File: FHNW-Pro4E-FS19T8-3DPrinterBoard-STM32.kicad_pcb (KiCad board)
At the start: 4 copper layers, 155 x 95 mm, 209 parts, among them J101 Screw_Terminal_01x02, J201 Micro_SD_Card_Det, J202 Conn_02x05_Odd_Even, J204 Conn_ARM_JTAG_SWD_10, J401 Conn_01x02, J402 Conn_01x02, J403 Screw_Terminal_01x02, J404 Conn_01x02, J405 Conn_01x02, J406 Screw_Terminal_01x02, J407 Conn_01x02, J408 Conn_01x02, J409 Conn_01x02, J410 Conn_01x02, J411 Conn_01x02, J504 USB_C_Receptacle, J601 B4B-XH-A, J602 B4B-XH-A, J603 B4B-XH-A, J604 B4B-XH-A, Q1 2N3904, Q2 2N3904, SW201 SW_Push, SW301 SW_Push, SW302 SW_Push, T401 BUK963R3-60E, T402 BUK963R3-60E, T403 BUK963R3-60E, T404 BUK963R3-60E, T405 BUK963R3-60E, U1 USBLC6-2SC6, U101 LM2675M-3.3, U102 LM2675M-5, U201 STM32F103ZETx, U202 NTS0104PW-Q100J, U203 NTS0104PW-Q100J, U301 ESP32-WROOM-32, U502 FT2232D, U601 TMC2660, U602 TMC2660, U603 TMC2660, U604 TMC2660, X201 SG-210STF, X501 SG5032CCN-6.000000M-HJGA3

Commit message: added cache.lib to git
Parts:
- added J203: Conn_02x20_Top_Bottom, Connector_PinHeader_2.54mm:PinHeader_2x20_P2.54mm_Vertical, F.Cu at (184.2, 113.0)
- added R217: 200R, Resistors_SMD:R_0603, F.Cu at (206.4, 26.0)
- J204: footprint Connectors_Multicomp:Multicomp_MC9A12-2034_2x10x2.54mm_Straight -> Connector_PinHeader_1.27mm:PinHeader_2x05_P1.27mm_Vertical
- U101: footprint Housings_SOIC:SOIC-8-1EP_3.9x4.9mm_Pitch1.27mm -> Package_SO:SOIC-8_3.9x4.9mm_P1.27mm
- moved J204 90.9 mm to (211.5, 22.2), turned to 270 degrees
- moved R204 34.8 mm to (207.6, 29.8), turned to 270 degrees
- moved R212 32.5 mm to (207.6, 26.0), turned to 270 degrees
- moved D103 31.8 mm to (146.1, 66.7)
- moved C109 31.7 mm to (149.2, 61.0)
- moved U102 31.7 mm to (145.4, 60.3)
- moved C107 31.7 mm to (137.8, 55.2)
- moved C108 31.7 mm to (137.8, 66.7)
- moved L102 31.7 mm to (155.6, 60.3)
- moved R101 28.6 mm to (108.0, 59.1)
- moved R210 28.6 mm to (211.5, 26.0), turned to 270 degrees
- moved D102 28.6 mm to (108.0, 62.9)
- moved R211 27.3 mm to (208.9, 26.0), turned to 270 degrees
- moved R201 22.6 mm to (206.4, 29.8), turned to 90 degrees
- moved R207 19.1 mm to (218.4, 97.8)
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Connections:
- J204 pad 10: JTAG_RESET -> Net-(J204-Pad10)
- R203 pad 1: Net-(J204-Pad2) -> JTAG_TMS_SWDIO
- R204 pad 1: Net-(J204-Pad8) -> JTAG_TDI
- R205 pad 2: Net-(J204-Pad4) -> JTAG_TCK_SWCLK
- R206 pad 2: Net-(J204-Pad6) -> JTAG_TDO_SWO
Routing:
- net +3V3: track 77.4 -> 172.2 mm
- net /appendix_TMC2660_X/TMC_CS_X: track 5.21 -> 31.0 mm
- net /appendix_STM32F103/CS_Y: track 5.21 -> 31.0 mm
- net /appendix_STM32F103/CS_Z1: track 5.21 -> 31.0 mm
- net /appendix_STM32F103/EN_Y: track 3.58 -> 27.5 mm
- net /appendix_STM32F103/EN_Z1: track 3.58 -> 27.5 mm
- net /appendix_TMC2660_X/TMC_EN_X: track 3.58 -> 27.5 mm
- net Net-(D102-Pad2): track 3.73 -> 0.00 mm
- net GND: track 182.8 -> 186.5 mm, vias 80 -> 76
- net JTAG_TMS_SWDIO: track 0.00 -> 2.31 mm, vias 0 -> 1
- net JTAG_TDO_SWO: track 0.00 -> 2.31 mm, vias 0 -> 1
- net JTAG_TDI: track 0.00 -> 2.31 mm, vias 0 -> 1
- net JTAG_TCK_SWCLK: track 0.00 -> 2.31 mm, vias 0 -> 1
- net JTAG_RESET: track 0.00 -> 2.31 mm, vias 0 -> 1
- net Net-(J204-Pad8): track 0.00 -> 1.79 mm
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
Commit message: cleaned up Layout
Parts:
- removed R202: 100k, Resistors_SMD:R_0603
- T401, T404, T405: value BUK963R3-60E -> PMV40UN2; footprint Package_TO_SOT_SMD:TO-263-2 -> Package_TO_SOT_SMD:SOT-23
- moved R102 194.6 mm to (108.0, 57.1), turned to 270 degrees
- moved D104 192.1 mm to (108.0, 61.0), turned to 90 degrees
- moved R422 177.1 mm to (50.8, 58.4)
- moved D405 140.0 mm to (147.3, 30.5)
- moved R423 138.9 mm to (78.1, 55.9)
- moved J409 108.7 mm to (154.3, 25.4)
- moved T404 107.7 mm to (157.5, 34.9)
- moved J401 105.5 mm to (162.6, 25.4)
- moved R506 105.1 mm to (222.2, 79.4), turned to 180 degrees
- moved T401 104.2 mm to (165.7, 34.9)
- moved R413 103.7 mm to (154.3, 38.1), turned to 0 degrees
- moved R404 100.3 mm to (162.6, 38.1), turned to 0 degrees
- moved T405 89.7 mm to (149.2, 34.9), turned to 90 degrees
- moved R420 84.4 mm to (146.1, 38.1)
- moved X201 78.0 mm to (172.1, 51.4), turned to 270 degrees
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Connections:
- C613 pad 1: +3V3 -> +3.3VP
- C615 pad 1: +3V3 -> +3.3VP
- C629 pad 1: +3V3 -> +3.3VP
- C631 pad 1: +3V3 -> +3.3VP
- T401 pad 2: /appendix_SENSORS_POWER/Fan1_pwr -> GND
- T401 pad 3: GND -> /appendix_SENSORS_POWER/Fan1_pwr
- T404 pad 2: /appendix_SENSORS_POWER/Fan2_pwr -> GND
- T404 pad 3: GND -> /appendix_SENSORS_POWER/Fan2_pwr
- T405 pad 2: /appendix_SENSORS_POWER/Fan3_pwr -> GND
- T405 pad 3: GND -> /appendix_SENSORS_POWER/Fan3_pwr
- U601 pad 40: +3V3 -> +3.3VP
- U602 pad 40: +3V3 -> +3.3VP
- U603 pad 40: +3V3 -> +3.3VP
- U604 pad 40: +3V3 -> +3.3VP
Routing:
- net +3.3VP: track 0.00 -> 121.1 mm, vias 0 -> 5
- net GND: track 186.5 -> 270.9 mm
- net +3V3: track 172.2 -> 90.6 mm, vias 4 -> 0
- net +24V: track 35.0 -> 20.4 mm
- net Net-(C302-Pad1): track 0.00 -> 12.4 mm
- net /appendix_ESP32/ESP32_RESET: track 25.1 -> 36.8 mm
- net /SW_Min_Z: track 0.00 -> 7.25 mm
- net /SW_End_Filament1: track 0.00 -> 7.25 mm
- net /SW_Min_X: track 0.00 -> 7.14 mm
- net /ADC_TEMP_E1: track 0.00 -> 7.14 mm
- net /SW_Min_Y: track 0.00 -> 7.14 mm
- net /ADC_TEMP_BED: track 0.00 -> 7.14 mm
- net +5V: track 46.2 -> 52.8 mm
- net JTAG_RESET: track 2.31 -> 6.41 mm
- net Net-(R503-Pad1): track 4.18 -> 8.21 mm
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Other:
- board size 155 x 95 mm -> 152 x 95 mm
- board text added: "Fan 3"
- board text added: "OPTIONS"
- board text added: "RESET"
- board text added: "Temp Bed"
- board text added: "Temp Ext"
- board text removed: "3D Printer"
- board text removed: "ADC Bed"
- board text removed: "ADC E1"

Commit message: Layout update
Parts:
- added D201: LED, LED_SMD:LED_0805_2012Metric, F.Cu at (156.7, 42.2)
- added H101: MountingHole, Mounting_Holes:MountingHole_3.2mm_M3_Pad, F.Cu at (86.0, 24.0)
- added H102: MountingHole, Mounting_Holes:MountingHole_3.2mm_M3_Pad, F.Cu at (86.0, 111.0)
- added H103: MountingHole, Mounting_Holes:MountingHole_3.2mm_M3_Pad, F.Cu at (236.0, 24.0)
- added H104: MountingHole, Mounting_Holes:MountingHole_3.2mm_M3_Pad, F.Cu at (236.0, 111.0)
- added R202: 330R, Resistors_SMD:R_0603, F.Cu at (160.7, 41.9)
- J203: value Conn_02x20_Top_Bottom -> Conn_02x20_Odd_Even
- moved R411 90.8 mm to (139.7, 47.0), turned to 0 degrees
- moved T403 79.6 mm to (129.1, 44.5), turned to 180 degrees
- moved R415 73.8 mm to (144.8, 44.5), turned to 180 degrees
- moved C407 70.5 mm to (141.6, 43.2), turned to 90 degrees
- moved TH401 68.3 mm to (139.1, 43.2), turned to 270 degrees
- moved R422 67.5 mm to (114.3, 35.6), turned to 180 degrees
- moved R416 56.5 mm to (114.3, 37.5), turned to 0 degrees
- moved D401 54.0 mm to (109.9, 37.5), turned to 0 degrees
- moved J406 50.8 mm to (104.8, 26.7)
- moved R417 37.8 mm to (95.9, 37.5), turned to 0 degrees
- moved D402 37.6 mm to (92.7, 37.5), turned to 0 degrees
- moved T402 36.9 mm to (111.1, 44.5), turned to 0 degrees
- moved F401 29.3 mm to (87.6, 48.3), turned to 0 degrees
- moved D403 29.3 mm to (134.6, 28.6)
- moved J401 29.3 mm to (133.4, 23.5)
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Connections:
- J203 pad 10: Net-(J203-Pad10) -> MISO
- J203 pad 11: Net-(J203-Pad11) -> SCK
- J203 pad 18: GND -> Net-(J203-Pad18)
- J203 pad 19: GND -> Net-(J203-Pad19)
- J203 pad 20: GND -> Net-(J203-Pad20)
- J203 pad 21: +24V -> Net-(J203-Pad21)
- J203 pad 22: +24V -> Net-(J203-Pad22)
- J203 pad 23: +5V -> Net-(J203-Pad23)
- J203 pad 24: +3V3 -> Net-(J203-Pad24)
- J203 pad 25: MISO -> Net-(J203-Pad25)
- J203 pad 3: +5V -> +24V
- J203 pad 35: Net-(J203-Pad35) -> GND
- J203 pad 36: Net-(J203-Pad36) -> GND
- J203 pad 37: Net-(J203-Pad37) -> GND
- J203 pad 4: +3V3 -> +24V
- J203 pad 5: MOSI -> +5V
- J203 pad 6: SCK -> +5V
- J203 pad 7: Net-(J203-Pad7) -> +3V3
- J203 pad 8: Net-(J203-Pad8) -> +3V3
- J203 pad 9: Net-(J203-Pad9) -> MOSI
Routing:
- net +24V: track 20.4 -> 208.5 mm
- net /POWER_BED: track 0.00 -> 90.4 mm
- net /appendix_TMC2660_X/TMC_STEP_X: track 3.92 -> 87.6 mm
- net /appendix_TMC2660_X/TMC_STALL_X: track 6.57 -> 87.8 mm
- net /appendix_TMC2660_X/TMC_DIR_X: track 5.91 -> 86.4 mm
- net /POWER_E1: track 0.00 -> 71.8 mm
- net /appendix_TMC2660_X/TMC_EN_X: track 27.5 -> 94.8 mm
- net JTAG_TMS_SWDIO: track 2.31 -> 68.8 mm, vias 1 -> 2
- net /appendix_TMC2660_X/TMC_CS_X: track 31.0 -> 97.0 mm
- net /appendix_STM32F103/STEP_Y: track 3.92 -> 64.5 mm
- net SD_DAT0: track 4.73 -> 64.7 mm, vias 1 -> 2
- net /appendix_STM32F103/STALL_Y: track 6.57 -> 64.8 mm
- net SD_DAT1: track 4.39 -> 62.4 mm, vias 1 -> 2
- net /appendix_STM32F103/DIR_Y: track 5.91 -> 63.3 mm
- net JTAG_TCK_SWCLK: track 2.31 -> 57.3 mm, vias 1 -> 2
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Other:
- board size 152 x 95 mm -> 158 x 95 mm
- net class Default: clearance 0.2 -> 0.1
- net class Power 24V added: clearance 0.2, trace_width 1.2, via_dia 1.4, via_drill 1
- net class thick removed
- rule trace_clearance: 0.2 -> 0.1
- board text added: "EXT"
- board text added: "RST"
- board text added: "SWD"
- board text removed: "E1"

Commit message: having issues with netclasses
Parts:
- added C110: TBD, Capacitors_SMD:C_0603, F.Cu at (109.9, 71.8)
- added C214: 100n, Capacitors_SMD:C_0603, F.Cu at (185.3, 42.0)
- added D105: D_Zener, Diodes_SMD:D_SMB, F.Cu at (109.9, 59.1)
- added R103: TBD, Resistors_SMD:R_0603, F.Cu at (106.0, 58.4)
- added T101: BUK963R3-60E, Package_TO_SOT_SMD:TO-263-2, F.Cu at (104.1, 66.0)
- moved C105 63.3 mm to (136.9, 1.27)
- moved C106 63.3 mm to (136.9, 2.54)
- moved FB102 63.3 mm to (134.3, 4.45)
- moved FB101 63.3 mm to (134.3, -0.64)
- moved D102 50.2 mm to (146.7, 51.1), turned to 180 degrees
- moved R101 45.8 mm to (142.9, 51.1), turned to 0 degrees
- moved F101 12.1 mm to (96.9, 57.1)
- moved C108 11.1 mm to (116.2, 66.7)
- moved C107 9.81 mm to (114.9, 55.2)
- moved R102 9.21 mm to (109.9, 53.7), turned to 180 degrees
- moved D104 8.67 mm to (106.0, 53.7), turned to 0 degrees
- moved D103 8.38 mm to (121.8, 66.7)
- moved L102 8.38 mm to (131.3, 60.3)
- moved C109 8.38 mm to (124.9, 61.0)
- moved U102 8.38 mm to (121.1, 60.3)
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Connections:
- net /ADC_TEMP_BED renamed /ADC_T_BED
- net /ADC_TEMP_E1 renamed /ADC_T_E1
- net /ADC_TEMP_PCB renamed /ADC_T_PCB
- net /POWER_BED renamed /BED_ON
- net /POWER_E1 renamed /E1_ON
- net Net-(J203-Pad12) renamed GPIO_EXT_0
- net Net-(J203-Pad13) renamed E3_CS
- net Net-(J203-Pad14) renamed E2_CS
- net Net-(J203-Pad15) renamed E3_STEP
- net Net-(J203-Pad16) renamed E2_STEP
- net Net-(J203-Pad17) renamed E3_DIR
- net Net-(J203-Pad18) renamed ES_DIR
- net Net-(J203-Pad19) renamed E3_EN
- net Net-(J203-Pad20) renamed E2_EN
- net Net-(J203-Pad21) renamed E3_STALL
- net Net-(J203-Pad22) renamed E2_STALL
- net Net-(J203-Pad23) renamed E3_END_FIL
- net Net-(J203-Pad24) renamed E2_END_FIL
- net Net-(J203-Pad25) renamed E3_ADC_TEMP
- net Net-(J203-Pad26) renamed E2_ADC_TEMP
- net Net-(J203-Pad27) renamed ADC_TEMP_EXT
- net Net-(J203-Pad28) renamed FAN_EXT
- net Net-(J203-Pad29) renamed GPIO_EXT_1
- net Net-(J203-Pad30) renamed E2_FAN1
- net Net-(J203-Pad31) renamed GPIO_EXT_2
- net Net-(J203-Pad32) renamed E2_FAN2
- net Net-(J203-Pad33) renamed GPIO_EXT_3
- net Net-(J203-Pad34) renamed E2_HOTEND
- net Net-(U201-Pad28) renamed /appendix_STM32F103/ADC_T_BED
- net Net-(U201-Pad29) renamed /appendix_STM32F103/ADC_T_E1
- net Net-(U201-Pad70) renamed /appendix_STM32F103/BED_ON
- F101 pad 2: Net-(F101-Pad2) -> Net-(C110-Pad1)
- J101 pad 1: Net-(F101-Pad2) -> Net-(J101-Pad1)
- J101 pad 2: GND -> Net-(C110-Pad1)
- J203 pad 5: +5V -> Net-(J203-Pad5)
- J203 pad 6: +5V -> Net-(J203-Pad6)
- R401 pad 1: +3V3 -> +3.3VA
- R405 pad 1: +3V3 -> +3.3VA
- R415 pad 1: +3V3 -> +3.3VA
- U201 pad 11: Net-(U201-Pad11) -> /appendix_STM32F103/CS_X
- U201 pad 12: Net-(U201-Pad12) -> /appendix_STM32F103/EN_X
- U201 pad 13: Net-(U201-Pad13) -> /appendix_STM32F103/STALL_X
- U201 pad 14: Net-(U201-Pad14) -> /appendix_STM32F103/DIR_X
- U201 pad 15: Net-(U201-Pad15) -> /appendix_STM32F103/STEP_X
- U201 pad 80: /appendix_STM32F103/CS_Z1 -> /appendix_STM32F103/STEP_Z1
- U201 pad 81: /appendix_STM32F103/EN_Z1 -> /appendix_STM32F103/DIR_Z1
- U201 pad 87: /appendix_STM32F103/STEP_Z1 -> /appendix_STM32F103/EN_Z1
- U201 pad 88: /appendix_STM32F103/DIR_Z1 -> /appendix_STM32F103/CS_Z1
- U602 pad 18: /appendix_TMC2660_X/TMC_CS_X -> /appendix_STM32F103/CS_X
- U602 pad 19: /appendix_TMC2660_X/TMC_EN_X -> /appendix_STM32F103/EN_X
- U602 pad 38: /appendix_TMC2660_X/TMC_STALL_X -> /appendix_STM32F103/STALL_X
- U602 pad 41: /appendix_TMC2660_X/TMC_DIR_X -> /appendix_STM32F103/DIR_X
- U602 pad 42: /appendix_TMC2660_X/TMC_STEP_X -> /appendix_STM32F103/STEP_X
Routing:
- net /appendix_STM32F103/CS_X: track 0.00 -> 155.0 mm, vias 0 -> 2
- net /appendix_STM32F103/EN_X: track 0.00 -> 151.3 mm, vias 0 -> 2
- net /appendix_STM32F103/STALL_X: track 0.00 -> 142.7 mm, vias 0 -> 2
- net /appendix_STM32F103/DIR_X: track 0.00 -> 140.1 mm, vias 0 -> 2
- net /appendix_STM32F103/STEP_X: track 0.00 -> 140.0 mm, vias 0 -> 2
- net /appendix_TMC2660_X/TMC_CS_X: track 97.0 -> 0.00 mm, vias 1 -> 0
- net /appendix_TMC2660_X/TMC_EN_X: track 94.8 -> 0.00 mm, vias 1 -> 0
- net /appendix_TMC2660_X/TMC_STALL_X: track 87.8 -> 0.00 mm, vias 1 -> 0
- net /appendix_TMC2660_X/TMC_STEP_X: track 87.6 -> 0.00 mm, vias 1 -> 0
- net /appendix_TMC2660_X/TMC_DIR_X: track 86.4 -> 0.00 mm, vias 1 -> 0
- net Net-(C110-Pad1): track 0.00 -> 55.8 mm
- net /appendix_STM32F103/EN_Y: track 56.3 -> 102.1 mm, vias 1 -> 2
- net /appendix_STM32F103/CS_Y: track 59.1 -> 103.8 mm, vias 1 -> 2
- net SCK: track 148.0 -> 191.9 mm, vias 5 -> 6
- net GND: track 313.7 -> 356.9 mm, vias 82 -> 97
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- added copper zone on F.Cu, net Net-(C110-Pad1)
- added copper zone on F.Cu, net Net-(J101-Pad1)
- removed copper zone on F.Cu, net Net-(F101-Pad2)

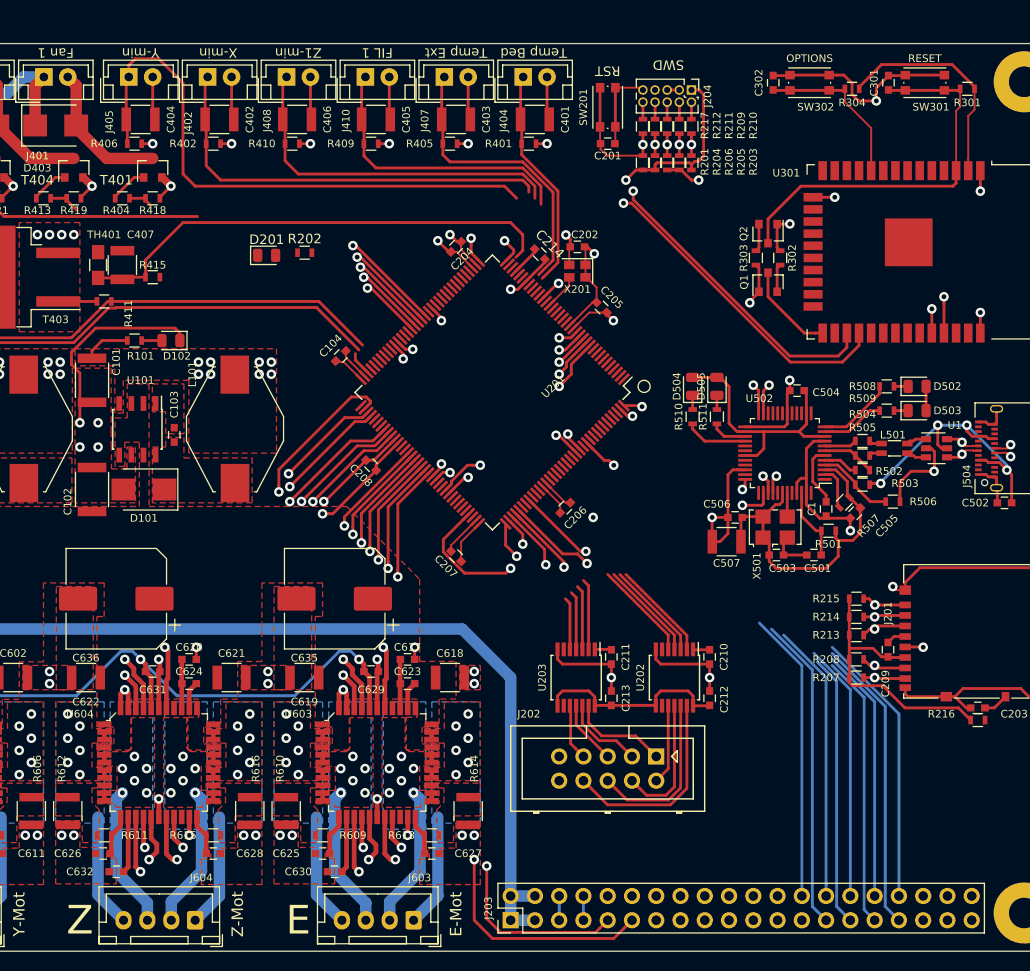
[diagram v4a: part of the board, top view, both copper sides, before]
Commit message: Layoutet Power 3.3V / 5V
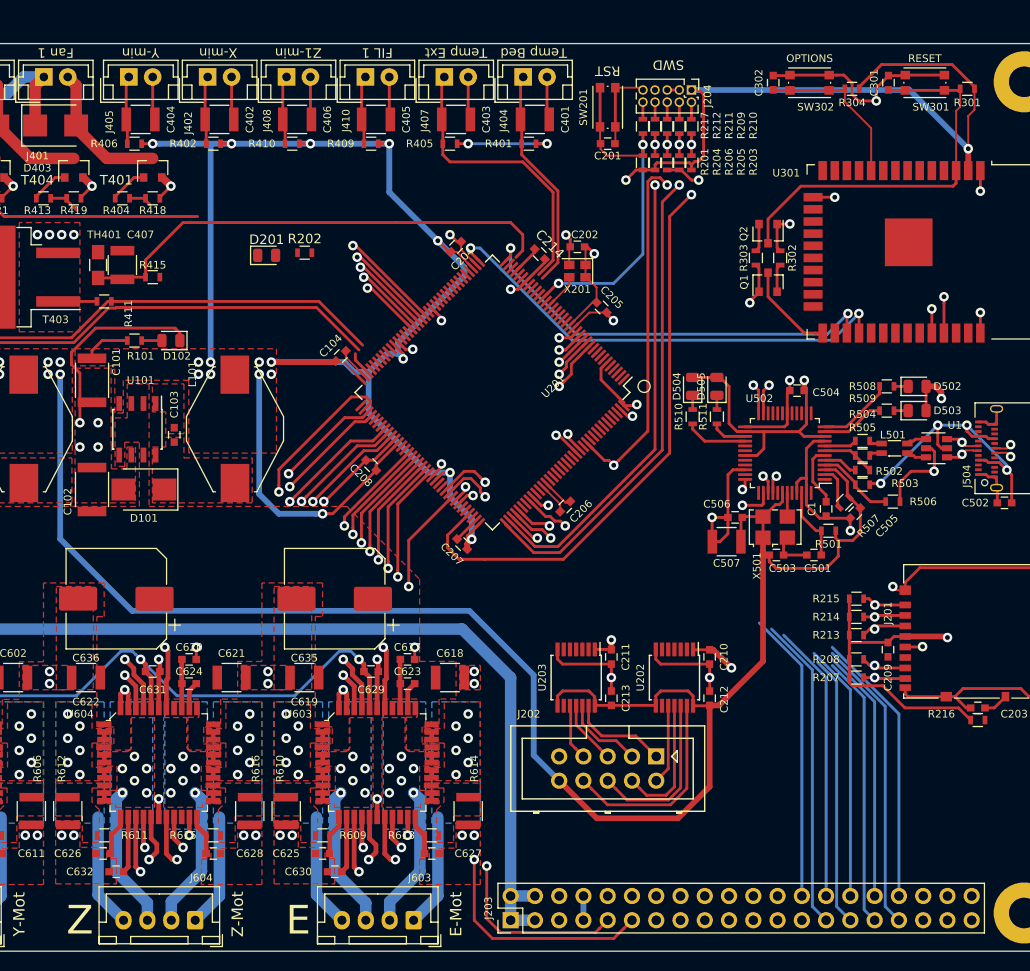
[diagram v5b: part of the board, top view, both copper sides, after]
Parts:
- moved C207 1.42 mm to (177.2, 72.4)
- moved C206 0.13 mm to (188.0, 68.5)
- turned C209 to 270 degrees
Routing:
- net +3V3: track 163.2 -> 574.6 mm, vias 20 -> 27
- net +5V: track 63.8 -> 193.3 mm
- net /SW_Min_Y: track 60.9 -> 7.14 mm
- net /SW_Min_X: track 44.7 -> 7.14 mm
- net /SW_Min_Z: track 37.6 -> 7.25 mm
- net /SW_End_Filament1: track 30.3 -> 7.25 mm
- net SD_DAT2: track 52.1 -> 64.1 mm, vias 3 -> 2
- net Net-(U201-Pad100): track 0.00 -> 11.3 mm, vias 0 -> 1
- net Net-(U202-Pad2): track 10.5 -> 0.00 mm
- net Net-(U202-Pad3): track 10.5 -> 0.00 mm
- net Net-(U202-Pad4): track 10.5 -> 0.00 mm
- net Net-(U202-Pad5): track 10.5 -> 0.00 mm
- net +3.3VA: track 5.45 -> 13.7 mm
- net Net-(U203-Pad2): track 7.43 -> 0.00 mm
- net Net-(U203-Pad3): track 6.79 -> 0.00 mm
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- removed copper zone on In1.Cu, net GND
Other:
- net class Power 5V added: clearance 0.1, trace_width 0.6, via_dia 1, via_drill 0.5
